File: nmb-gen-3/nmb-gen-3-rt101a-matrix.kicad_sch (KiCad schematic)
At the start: 200 parts

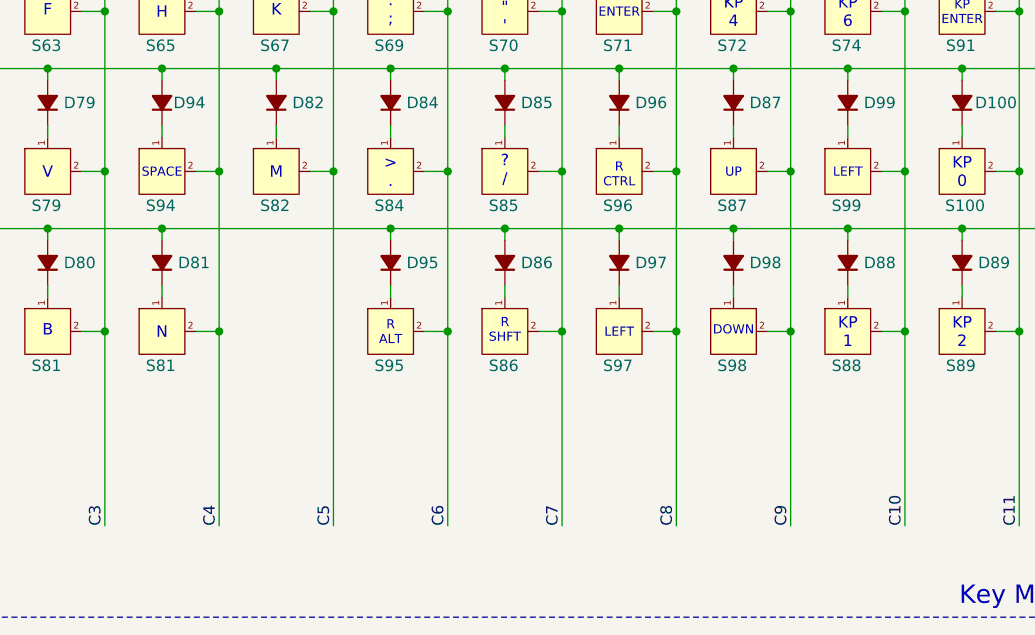
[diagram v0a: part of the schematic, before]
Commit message: Update nmb-gen-3-rt101a-matrix.kicad_sch
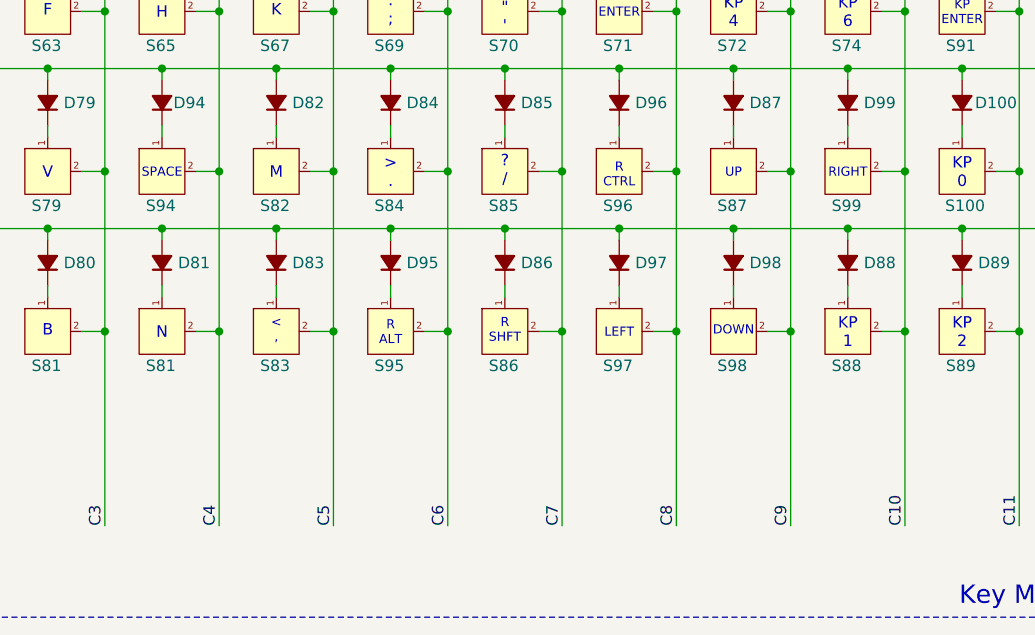
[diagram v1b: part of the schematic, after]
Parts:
- added D83: D_Small_Filled, symbol Device:D_Small_Filled
- added S83: nmb-si-725_4pin, symbol nmb-at-84:SW_Push_RightAngle
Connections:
- net C5: now also S83.2
- net R7: now also D83.2 (A)
- new net: D83.1 (K), S83.1
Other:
- note added: "< ,"
- note added: "RIGHT"
